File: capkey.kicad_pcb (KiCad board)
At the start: 2 copper layers, 44 x 29 mm, 19 parts, among them J1 TIP, J2 RING, J3 AudioJack4, Q1 Q_NMOS_DGS, Q2 Q_NMOS_DGS, SW1 SW_SPDT, U1 AT42QT1011-TSHR, U2 AT42QT1011-TSHR, U3 L78L05_SOT89

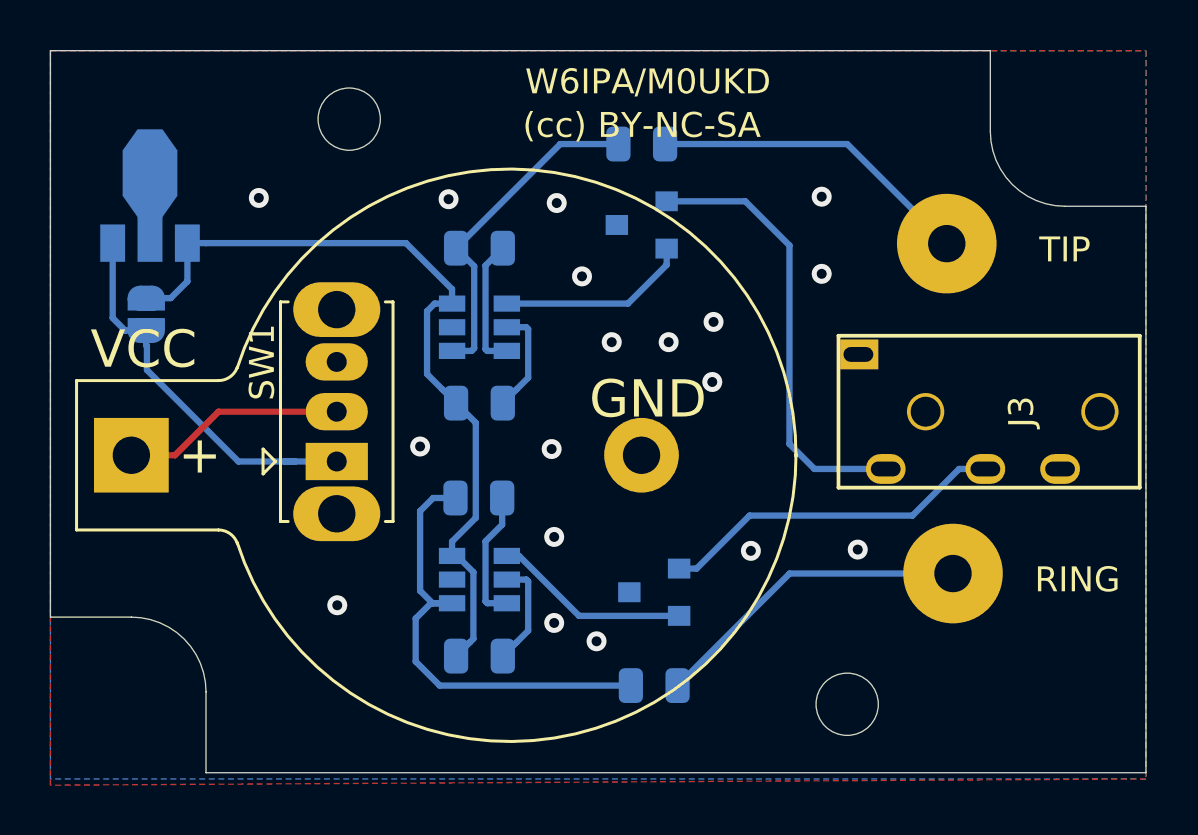
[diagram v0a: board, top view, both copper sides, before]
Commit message: Added attiny keyer
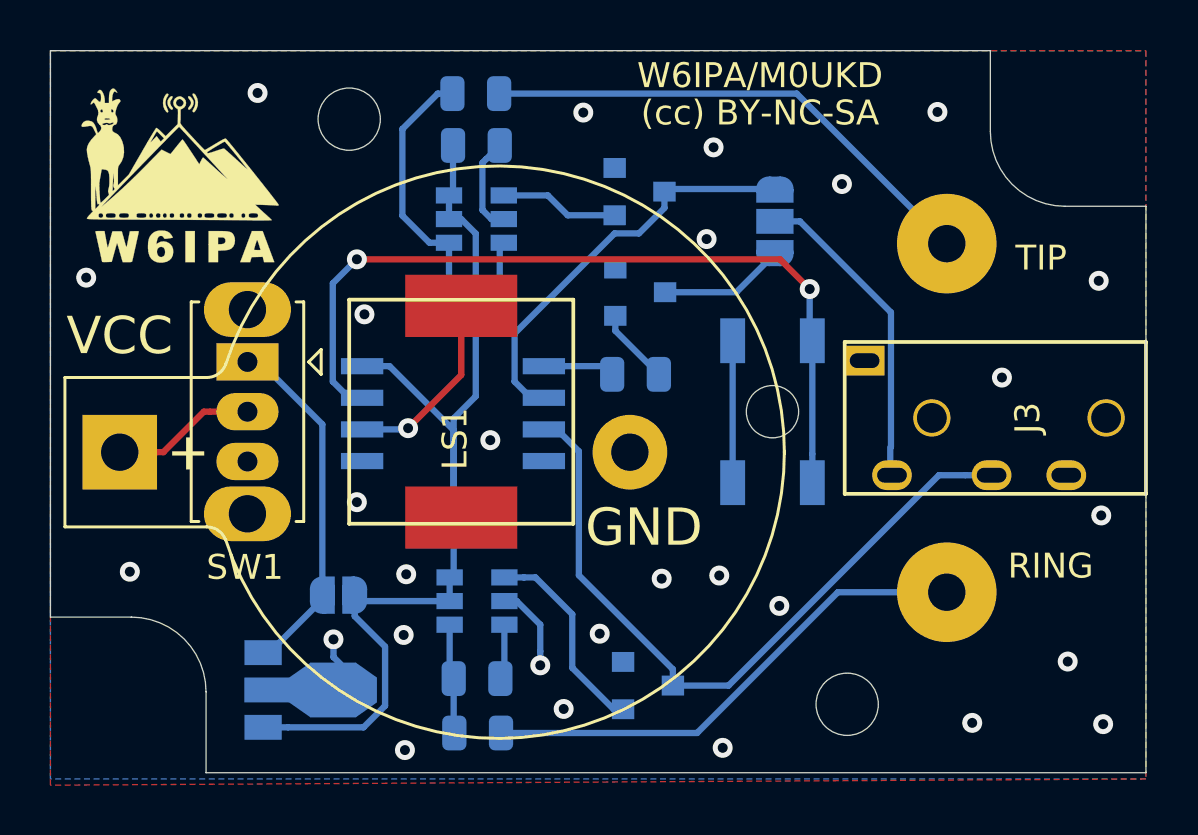
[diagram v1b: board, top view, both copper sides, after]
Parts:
- added H3: MountingHole, MountingHole:MountingHole_2.1mm, F.Cu at (167.9, 44.5)
- added JP2: SolderJumper_3_Open, Jumper:SolderJumper-3_P1.3mm_Open_RoundedPad1.0x1.5mm, B.Cu at (168.1, 36.9)
- added LOGO1: dahu-logo, w6ipa-footprints:W6IPA-Logo-9mmx8mm, F.Cu at (144.5, 35.3)
- added LS1: Speaker_Crystal, w6ipa-footprints:CPT-9019S-SMT-TR, F.Cu at (155.5, 40.0)
- added Q3: Q_NMOS_GSD, Package_TO_SOT_SMD:SOT-23, B.Cu at (162.7, 39.7)
- added R3: 1k, Resistor_SMD:R_0805_2012Metric, B.Cu at (162.5, 43.0)
- added SW2: SW_SPST, w6ipa-footprints:SW_Push_1P1T_NO_CK_PTS647, B.Cu at (168.0, 44.5)
- added U4: ATtiny85V-10SU, Package_SO:SOIJ-8_5.3x5.3mm_P1.27mm, B.Cu at (155.2, 44.6)
- Q1, Q2: value Q_NMOS_DGS -> Q_NMOS_GSD
- moved U3 20.3 mm to (149.0, 55.7), turned to 0 degrees
- moved JP1 13.7 mm to (150.6, 51.9), turned to 0 degrees
- moved C3 10.3 mm to (156.1, 33.8)
- moved R2 7.34 mm to (156.2, 57.4)
- moved C4 7.25 mm to (156.1, 55.2)
- moved R1 6.97 mm to (156.1, 31.7)
- moved SW1 5.37 mm to (146.9, 42.5), turned to 270 degrees
- moved C2 5.12 mm to (156.1, 49.2)
- moved U1 4.35 mm to (156.1, 36.8)
- moved Q2 3.76 mm to (163.0, 55.5), turned to 0 degrees
- moved C1 1.87 mm to (156.1, 39.8)
- moved Q1 1.34 mm to (162.7, 35.7), turned to 0 degrees
- moved U2 0.87 mm to (156.1, 52.1)
- moved J2 0.79 mm to (175.0, 51.8)
- moved BT1 0.48 mm to (141.8, 46.1)
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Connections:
- net Net-(C2-Pad1) renamed VCC
- J3 pad T: tip -> Net-(J3-PadT)
- Q1 pad 1: tip -> Net-(Q1-Pad1)
- Q1 pad 2: Net-(Q1-Pad2) -> sleeve
- Q1 pad 3: sleeve -> tip
- Q2 pad 1: ring -> Net-(Q2-Pad1)
- Q2 pad 2: Net-(Q2-Pad2) -> sleeve
- Q2 pad 3: sleeve -> ring
- U1 pad 1: Net-(Q1-Pad2) -> Net-(Q1-Pad1)
- U2 pad 1: Net-(Q2-Pad2) -> Net-(Q2-Pad1)
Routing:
- net Net-(SW2-Pad2): track 0.00 -> 33.3 mm, vias 0 -> 2
- net ring: track 14.0 -> 29.0 mm
- net Net-(C4-Pad2): track 18.8 -> 4.43 mm
- net Net-(J3-PadT): track 0.00 -> 12.4 mm
- net VCC: track 32.4 -> 41.3 mm
- net Net-(Q2-Pad1): track 0.00 -> 8.22 mm
- net Net-(Q2-Pad2): track 7.92 -> 0.00 mm
- net Net-(Q1-Pad2): track 7.72 -> 0.00 mm
- net Net-(LS1-Pad1): track 0.00 -> 7.66 mm, vias 0 -> 1
- net Net-(J1-Pad1): track 13.0 -> 20.5 mm
- net Net-(J2-Pad1): track 12.9 -> 20.2 mm
- net sleeve: track 8.59 -> 15.6 mm, vias 18 -> 28
- net key: track 0.00 -> 5.05 mm
- net Net-(Q1-Pad1): track 0.00 -> 4.78 mm
- net +3V0: track 8.97 -> 5.80 mm
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
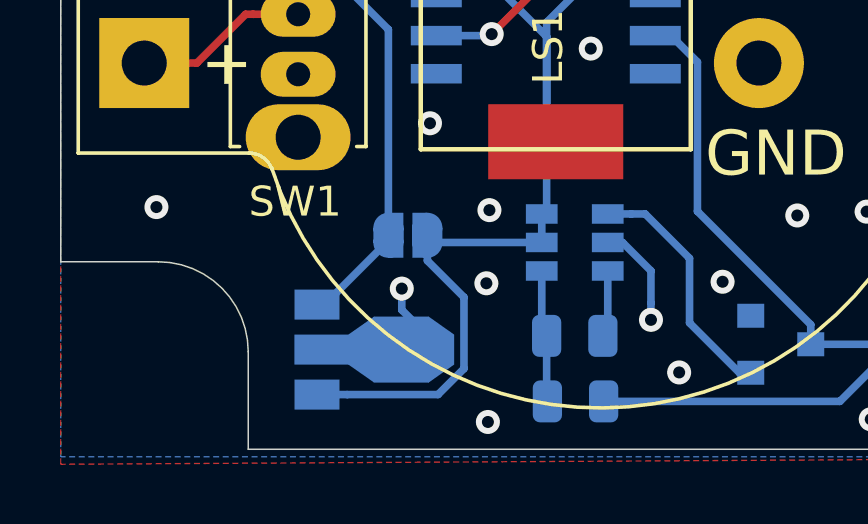
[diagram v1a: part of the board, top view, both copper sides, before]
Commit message: 7805 -> 7833
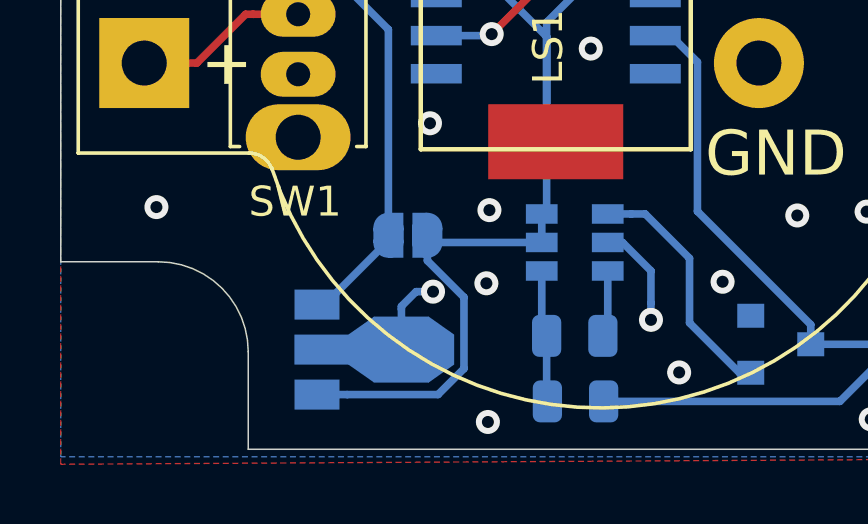
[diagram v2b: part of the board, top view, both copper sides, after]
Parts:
- U3: value L78L05_SOT89 -> L78L33_SOT89
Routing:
- net sleeve: track 15.6 -> 17.1 mm
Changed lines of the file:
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@@
     (thickness 1.6)
     (drawings 16)
-    (tracks 148)
+    (tracks 151)
     (zones 0)
     (modules 27)
@@
       (effects (font (size 1 1) (thickness 0.15)) (justify mirror))
     )
-    (fp_text value L78L05_SOT89 (at 0.45 -3.25) (layer B.Fab)
+    (fp_text value L78L33_SOT89 (at 0.45 -3.25) (layer B.Fab)
       (effects (font (size 1 1) (thickness 0.15)) (justify mirror))
     )
@@
   (segment (start 158.6738 53.052598) (end 158.6738 54.120515) (width 0.254) (layer B.Cu) (net 2))
   (segment (start 157.2338 52.1062) (end 157.727402 52.1062) (width 0.254) (layer B.Cu) (net 2))
-  (via (at 150.368 53.6448) (size 0.8) (drill 0.4) (layers F.Cu B.Cu) (net 2))
+  (via (at 151.4094 53.7464) (size 0.8) (drill 0.4) (layers F.Cu B.Cu) (net 2))
   (via (at 165.354 37.5666) (size 0.8) (drill 0.4) (layers F.Cu B.Cu) (net 2))
   (via (at 174.625 32.4612) (size 0.8) (drill 0.4) (layers F.Cu B.Cu) (net 2))
   (via (at 170.7896 35.3568) (size 0.8) (drill 0.4) (layers F.Cu B.Cu) (net 2))
-  (segment (start 150.368 54.356) (end 150.368 53.6448) (width 0.254) (layer B.Cu) (net 2))
-  (segment (start 151.6888 55.6768) (end 150.368 54.356) (width 0.254) (layer B.Cu) (net 2))
   (via (at 147.32 31.6992) (size 0.8) (drill 0.4) (layers F.Cu B.Cu) (net 2))
   (via (at 140.4366 39.116) (size 0.8) (drill 0.4) (layers F.Cu B.Cu) (net 2))
@@
   (via (at 153.289 51.0286) (size 0.8) (drill 0.4) (layers F.Cu B.Cu) (net 2))
   (via (at 159.6136 56.4388) (size 0.8) (drill 0.4) (layers F.Cu B.Cu) (net 2))
+  (segment (start 150.3553 55.6768) (end 151.6888 55.6768) (width 0.254) (layer B.Cu) (net 2))
+  (segment (start 150.3553 54.234815) (end 150.3553 54.3228) (width 0.254) (layer B.Cu) (net 2))
+  (segment (start 150.843715 53.7464) (end 150.3553 54.234815) (width 0.254) (layer B.Cu) (net 2))
+  (segment (start 150.3553 54.3228) (end 150.3553 55.6768) (width 0.254) (layer B.Cu) (net 2))
+  (segment (start 151.4094 53.7464) (end 150.843715 53.7464) (width 0.254) (layer B.Cu) (net 2))
   (segment (start 154.558 31.7246) (end 153.1366 33.146) (width 0.254) (layer B.Cu) (net 3))
   (segment (start 155.1455 31.7246) (end 154.558 31.7246) (width 0.254) (layer B.Cu) (net 3))
